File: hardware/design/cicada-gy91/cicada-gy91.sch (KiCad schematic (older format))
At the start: 3 parts, among them J1 Expansion slot1, J2 Expansion slot2, J3 GY-91 Module

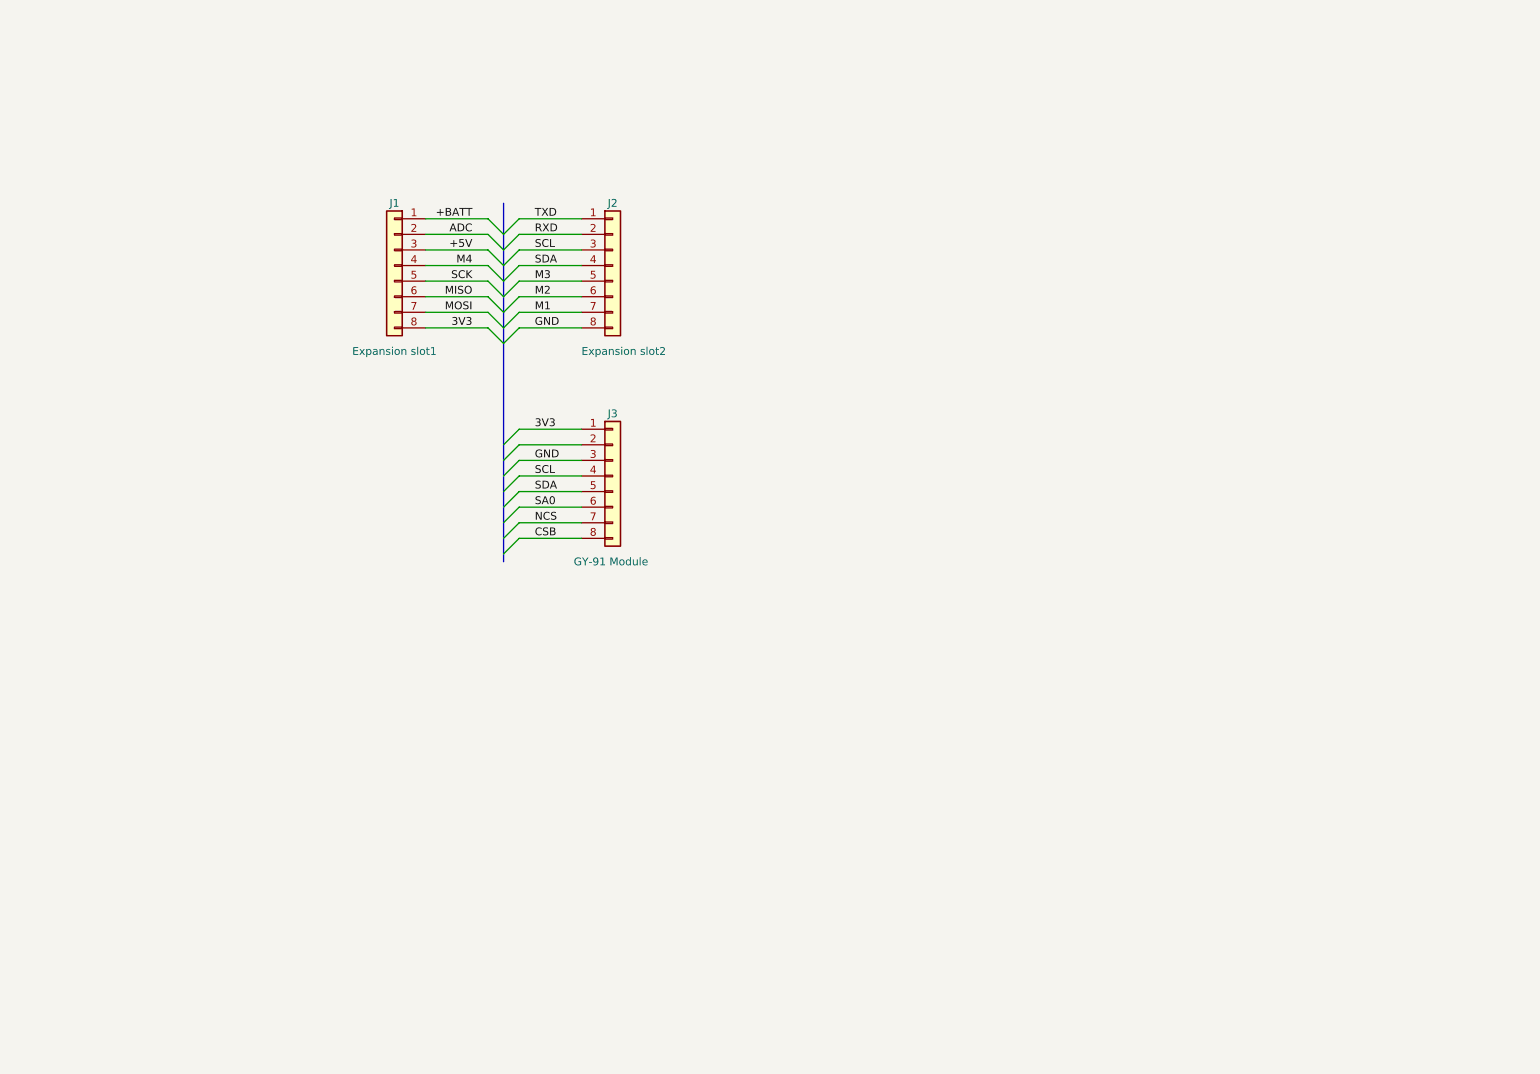
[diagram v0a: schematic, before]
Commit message: added new board cicada-gy91-v3
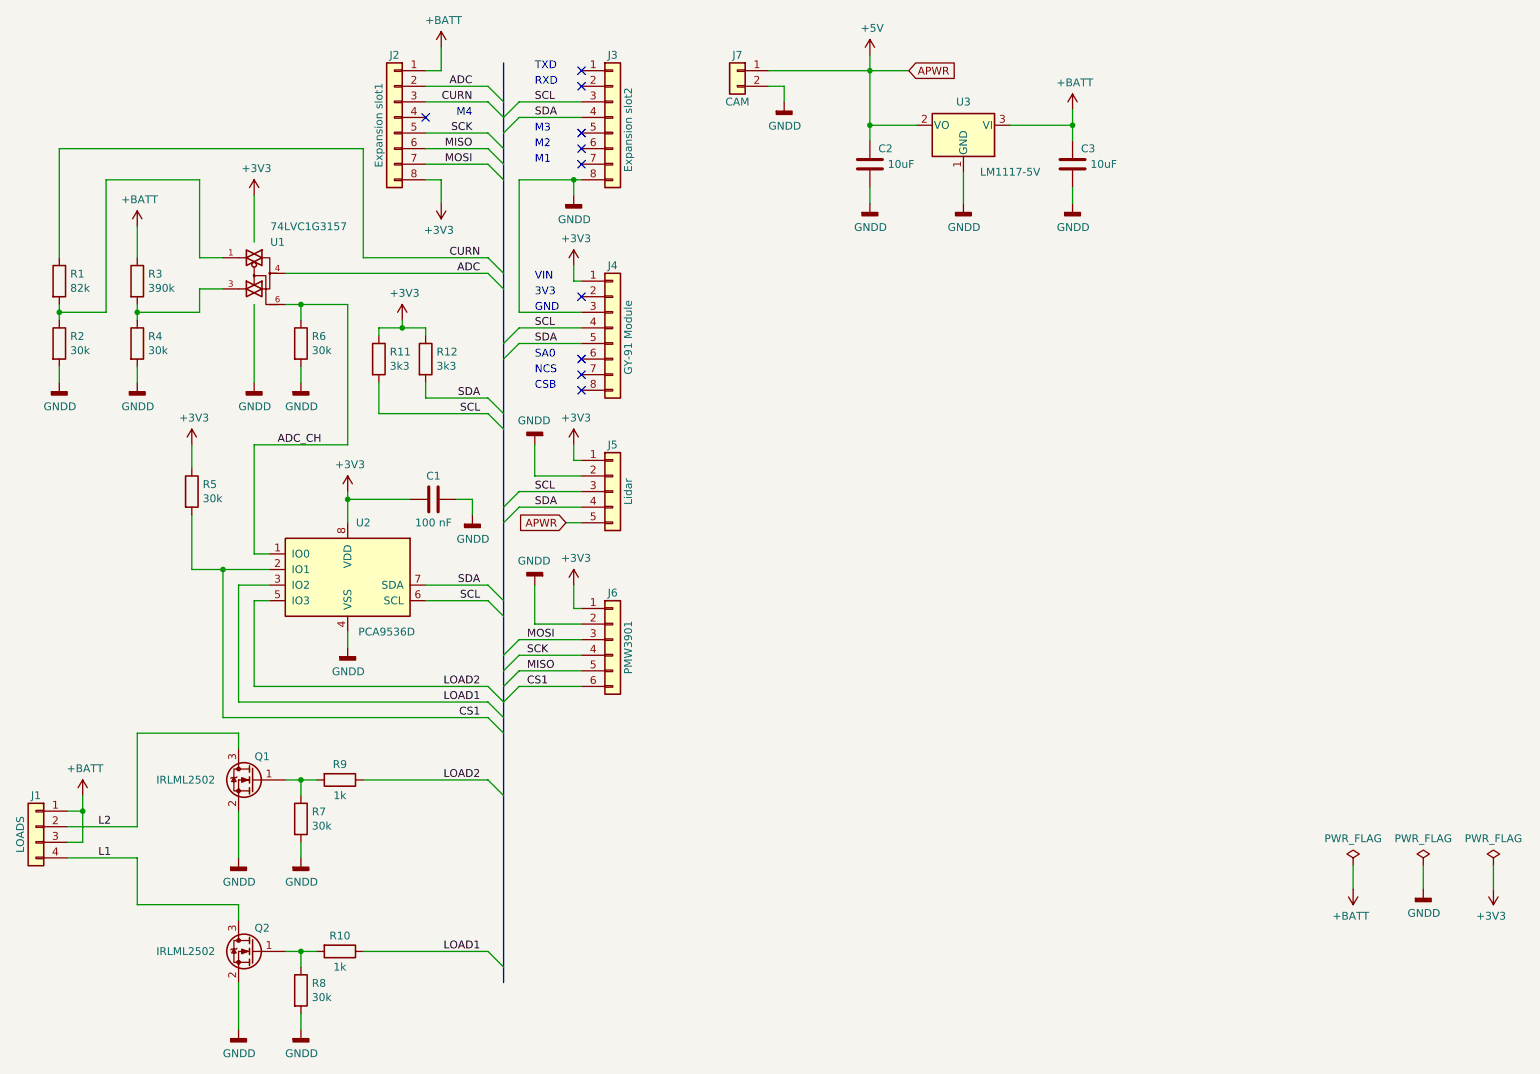
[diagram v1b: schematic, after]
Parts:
- added C1: 100 nF, Capacitor_SMD:C_0805_2012Metric, symbol Device:C
- added C2, C3: 10uF, Capacitor_SMD:C_0805_2012Metric, symbol Device:C
- added J1: LOADS, Connector_Molex:Molex_PicoBlade_53048-0810_1x04_P1.25mm_Horizontal, symbol Connector_Generic:Conn_01x04
- added J5: Lidar, Connector_Molex:Molex_PicoBlade_53048-1010_1x05_P1.25mm_Horizontal, symbol Connector_Generic:Conn_01x05
- added J6: PMW3901, Connector_Molex:Molex_PicoBlade_53048-1210_1x06_P1.25mm_Horizontal, symbol Connector_Generic:Conn_01x06
- added J7: CAM, Connector_Molex:Molex_PicoBlade_53048-0410_1x02_P1.25mm_Horizontal, symbol Connector_Generic:Conn_01x02
- added Q1, Q2: IRLML2502, Package_TO_SOT_SMD:SOT-23, symbol Transistor_FET:BSS138
- added R1: 82k, Resistor_SMD:R_0805_2012Metric, symbol Device:R
- added R10, R9: 1k, Resistor_SMD:R_0805_2012Metric, symbol Device:R
- added R11, R12: 3k3, Resistor_SMD:R_0805_2012Metric, symbol Device:R
- added R2, R4, R5, R6, R7, R8: 30k, Resistor_SMD:R_0805_2012Metric, symbol Device:R
- added R3: 390k, Resistor_SMD:R_0805_2012Metric, symbol Device:R
- added U1: 74LVC1G3157, Package_TO_SOT_SMD:SOT-363_SC-70-6, symbol 74xGxx:74LVC1G3157
- added U2: PCA9536D, Package_SO:SOIC-8_3.9x4.9mm_P1.27mm, symbol Interface_Expansion:PCA9536D
- added U3: LM1117-5V, Package_TO_SOT_SMD:SOT-223, symbol Regulator_Linear:LM1117-3.3
- renumbered J1 to J2, J2 to J3, J3 to J4
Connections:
- net +5V: now also C2.2, J5.5 (Pin_5), J7.1 (Pin_1), U3.2 (VO); no longer J2.3 (Pin_3)
- net +BATT: now also C3.2, J1.1 (Pin_1), J1.3 (Pin_3), R3.1, U3.3 (VI)
- net ADC: now also U1.4
- net GND: now also C1.1, C2.1, C3.1, J5.2 (Pin_2), J6.2 (Pin_2), J7.2 (Pin_2), Q1.2 (S), Q2.2 (S), R2.2, R4.2, R6.2, R7.2, R8.2, U1.2 (GND), U2.4 (VSS), U3.1 (GND)
- net MISO: now also J6.5 (Pin_5)
- net MOSI: now also J6.3 (Pin_3)
- net SCK: now also J6.4 (Pin_4)
- net SCL: now also J5.3 (Pin_3), R11.2, U2.6 (SCL)
- net SDA: now also J5.4 (Pin_4), R12.2, U2.7 (SDA)
- net 3V3 renamed +3V3
- net +3V3: now also C1.2, J5.1 (Pin_1), J6.1 (Pin_1), R11.1, R12.1, R5.1, U1.5 (VCC), U2.8 (VDD)
- net CSB: no longer names the net of J4.8 (Pin_8)
- net M1: no longer names the net of J3.7 (Pin_7)
- net M2: no longer names the net of J3.6 (Pin_6)
- net M3: no longer names the net of J3.5 (Pin_5)
- net M4: no longer names the net of J2.4 (Pin_4)
- net NCS: no longer names the net of J4.7 (Pin_7)
- net RXD: no longer names the net of J3.2 (Pin_2)
- net SA0: no longer names the net of J4.6 (Pin_6)
- net TXD: no longer names the net of J3.1 (Pin_1)
- new net: R1.2, R2.1, U1.1
- new net: R3.2, R4.1, U1.3
- new net: Q1.1 (G), R7.1, R9.2
- new net: Q2.1 (G), R10.2, R8.1
- new net ADC_CH: R6.1, U1.6, U2.1 (IO0)
- new net CS1: J6.6 (Pin_6), R5.2, U2.2 (IO1)
- new net CURN: J2.3 (Pin_3), R1.1
- new net L1: J1.4 (Pin_4), Q2.3 (D)
- new net L2: J1.2 (Pin_2), Q1.3 (D)
- new net LOAD1: R10.1, U2.3 (IO2)
- new net LOAD2: R9.1, U2.5 (IO3)
- no-connect marks 0 -> 10
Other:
- note added: "3V3"
- note added: "CSB"
- note added: "GND"
- note added: "M1"
- note added: "M2"
- note added: "M3"
- note added: "M4"
- note added: "NCS"
- note added: "RXD"
- note added: "SA0"
- note added: "TXD"
- note added: "VIN"
- moved on the sheet: J2, J3, J4
